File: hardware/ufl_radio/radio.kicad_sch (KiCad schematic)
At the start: 28 parts, among them J2 U.FL, J3 Shield, U1 MAX2769B

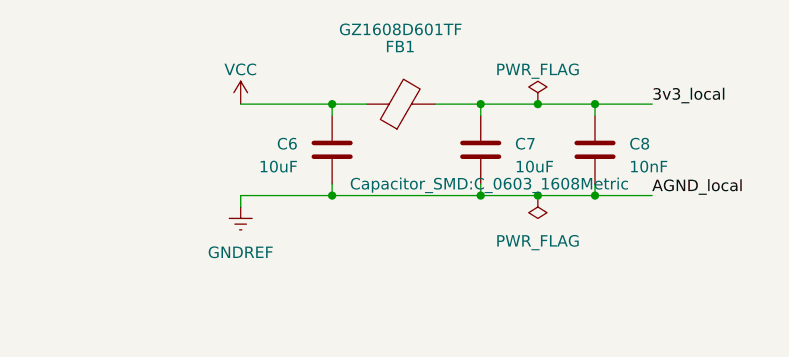
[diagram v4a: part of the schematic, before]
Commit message: Update and improve noise on ufl radio
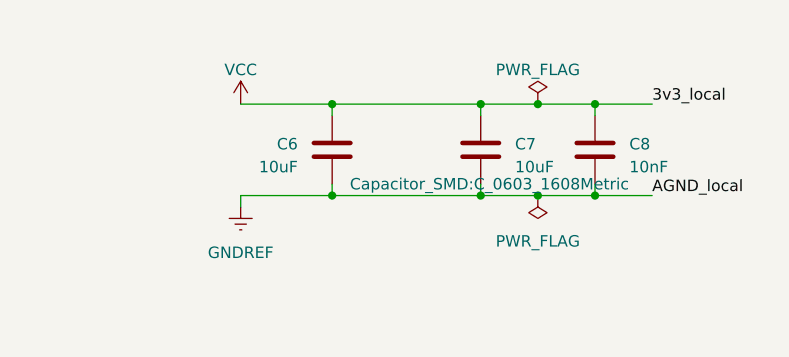
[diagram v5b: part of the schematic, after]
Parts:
- removed FB1: GZ1608D601TF, Inductor_SMD:L_0603_1608Metric, symbol Device:FerriteBead
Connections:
- net 3v3_local is gone; now on net VCC: C1.1, C10.1, C12.1, C13.1, C15.1, C3.1, C7.1, C8.1, C9.1, D1.2 (A), U1.11 (VCC_VCO), U1.13 (VCC_CP), U1.14 (VCCD), U1.19 (VCC_ADC), U1.23 (VCC_IF), U1.24 (IDLE#), U1.4 (VCC_RF)
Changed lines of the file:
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@@
-	(wire
-		(pts
-			(xy 241.3 27.94) (xy 246.38 27.94)
-		)
-		(stroke
-			(width 0)
-			(type default)
-		)
-	)
 	(wire
 		(pts
@@
 	(wire
 		(pts
-			(xy 229.87 27.94) (xy 233.68 27.94)
+			(xy 229.87 27.94) (xy 246.38 27.94)
 		)
 		(stroke
@@
 					(unit 1)
 				)
-			)
-		)
-	)
-	(symbol
-		(lib_id "Device:FerriteBead")
-		(at 237.49 27.94 90)
-		(unit 1)
-		(exclude_from_sim no)
-		(in_bom yes)
-		(on_board yes)
-		(dnp no)
-		(property "Reference" "FB1"
-			(at 237.4392 21.59 90)
-			(effects
-				(font
-					(size 1.27 1.27)
-				)
-			)
-		)
-		(property "Value" "GZ1608D601TF"
-			(at 237.49 19.685 90)
-			(effects
-				(font
-					(size 1.27 1.27)
-				)
-			)
-		)
-		(property "Footprint" "Inductor_SMD:L_0603_1608Metric"
-			(at 237.49 29.718 90)
-			(effects
-				(font
-					(size 1.27 1.27)
-				)
-				(hide yes)
-			)
-		)
-		(property "Datasheet" "~"
-			(at 237.49 27.94 0)
-			(effects
-				(font
-					(size 1.27 1.27)
-				)
-				(hide yes)
-			)
-		)
-		(property "Description" "Ferrite bead"
-			(at 237.49 27.94 0)
-			(effects
-				(font
-					(size 1.27 1.27)
-				)
-				(hide yes)
-			)
-		)
-		(property "LCSC" "C1002"
-			(at 237.49 27.94 90)
-			(effects
-				(font
-					(size 1.27 1.27)
-				)
-				(hide yes)
-			)
-		)
-		(pin "1"
-		)
-		(pin "2"
-		)
-		(instances
-			(project "design"
-				(path "/6dbd6c42-edf6-461d-b7ca-066e49b0019c/1b895c4a-56fd-4590-a8aa-7507dccb37cf"
-					(reference "FB2")
-					(unit 1)
-				)
-				(path "/6dbd6c42-edf6-461d-b7ca-066e49b0019c/78691f3e-c8cc-4de2-b4f7-4d5d660bca23"
-					(reference "FB1")
-					(unit 1)
-				)
-				(path "/6dbd6c42-edf6-461d-b7ca-066e49b0019c/bbad701b-ab9c-48bf-af04-0d262cb749b1"
-					(reference "FB3")
-					(unit 1)
-				)
-				(path "/6dbd6c42-edf6-461d-b7ca-066e49b0019c/f20fbf31-47b8-4912-9caa-c1ed256d71c4"
-					(reference "FB4")
-					(unit 1)
-				)
